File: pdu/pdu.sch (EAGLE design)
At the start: 54 parts, among them IC1 FDN359BN, IC2 FDN359BN, IC3 FDN359BN, J1 S2B-PH-K-S(LF)(SN), J10 S2B-PH-K-S(LF)(SN), J2 S2B-PH-K-S(LF)(SN), J3 S2B-PH-K-S(LF)(SN), J4 S2B-PH-K-S(LF)(SN), J5 S2B-PH-K-S(LF)(SN), J6 S2B-PH-K-S(LF)(SN), J7 S2B-PH-K-S(LF)(SN), J8 S2B-PH-K-S(LF)(SN), J9 S2B-PH-K-S(LF)(SN)

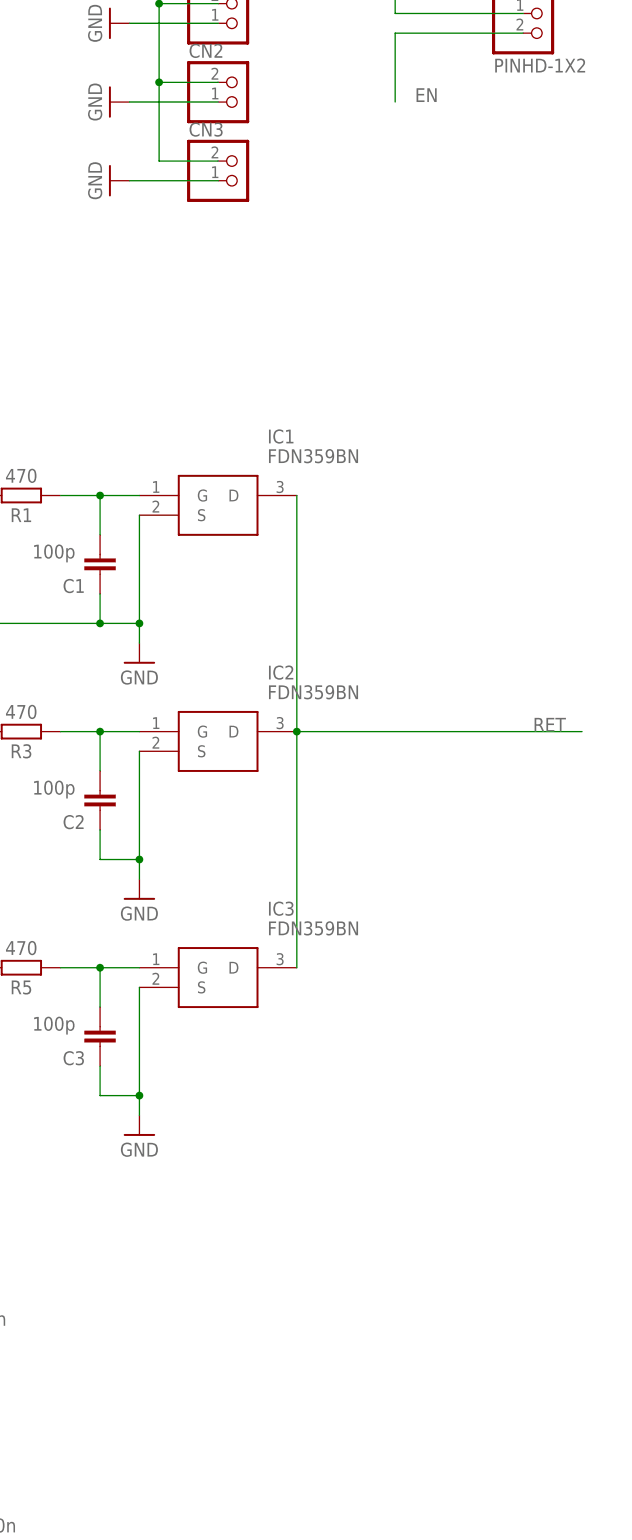
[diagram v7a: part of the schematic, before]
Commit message: add status leds
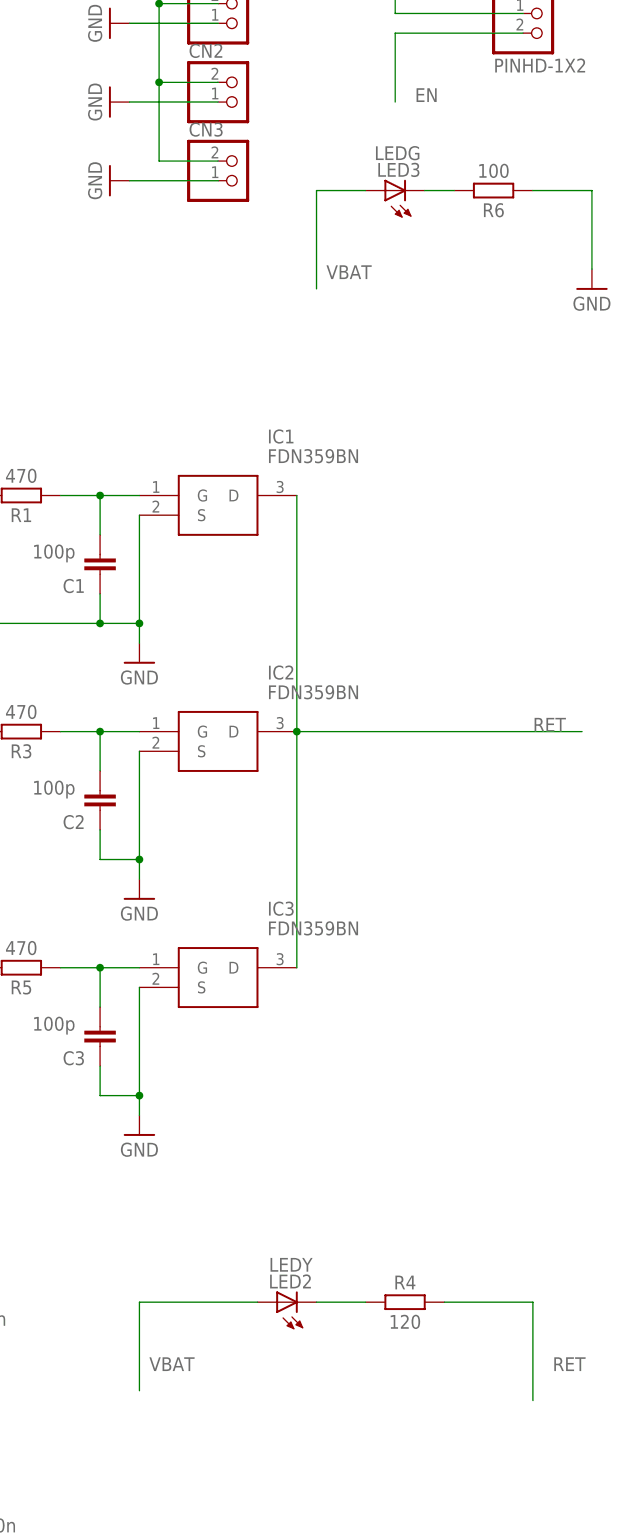
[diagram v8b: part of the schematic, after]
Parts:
- added LED2: LEDY, adafruit:LEDCHIPLED_0805
- added LED3: LEDG, adafruit:LEDCHIPLED_0805
- added R4: 120, Resistor:R_CHIP-0603(1608-METRIC)
- added R6: 100, Resistor:R_CHIP-0603(1608-METRIC)
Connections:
- new net N$4: LED3.C, R6.2
- new net N$5: LED2.C, R4.1
- net GND: now also R6.1
- net RET: now also R4.2
- net VBAT: now also LED2.A, LED3.A
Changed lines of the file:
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@@
 <part name="J9" library="Connectors" library_urn="urn:adsk.eagle:library:28493002" deviceset="S2B-PH-K-S(LF)(SN)" device="" package3d_urn="urn:adsk.eagle:package:10989924/2"/>
 <part name="J10" library="Connectors" library_urn="urn:adsk.eagle:library:28493002" deviceset="S2B-PH-K-S(LF)(SN)" device="" package3d_urn="urn:adsk.eagle:package:10989924/2"/>
+<part name="LED2" library="adafruit" library_urn="urn:adsk.eagle:library:420" deviceset="LED" device="CHIPLED_0805" package3d_urn="urn:adsk.eagle:package:6240559/1" value="LEDY"/>
+<part name="R4" library="Resistor" library_urn="urn:adsk.eagle:library:16378527" deviceset="R" device="CHIP-0603(1608-METRIC)" package3d_urn="urn:adsk.eagle:package:16378565/5" technology="_" value="120"/>
+<part name="R6" library="Resistor" library_urn="urn:adsk.eagle:library:16378527" deviceset="R" device="CHIP-0603(1608-METRIC)" package3d_urn="urn:adsk.eagle:package:16378565/5" technology="_" value="100"/>
+<part name="LED3" library="adafruit" library_urn="urn:adsk.eagle:library:420" deviceset="LED" device="CHIPLED_0805" package3d_urn="urn:adsk.eagle:package:6240559/1" value="LEDG"/>
+<part name="SUPPLY7" library="Power_Symbols" library_urn="urn:adsk.eagle:library:16502351" deviceset="GND-BAR" device="" value="GND"/>
 </parts>
 <sheets>
@@
 <attribute name="NAME" x="2.54" y="-235.712" size="1.778" layer="95" rot="R180"/>
 <attribute name="VALUE" x="2.54" y="-224.79" size="1.778" layer="96" rot="R180"/>
+</instance>
+<instance part="LED2" gate="G$1" x="17.78" y="-104.14" smashed="yes" rot="R90">
+<attribute name="NAME" x="22.352" y="-100.584" size="1.778" layer="95" rot="R180"/>
+<attribute name="VALUE" x="22.352" y="-98.425" size="1.778" layer="96" rot="R180"/>
+</instance>
+<instance part="R4" gate="G$1" x="34.29" y="-104.14" smashed="yes">
+<attribute name="NAME" x="34.29" y="-101.6" size="1.778" layer="95" align="center"/>
+<attribute name="VALUE" x="34.29" y="-106.68" size="1.778" layer="96" align="center"/>
+</instance>
+<instance part="R6" gate="G$1" x="45.72" y="39.37" smashed="yes" rot="R180">
+<attribute name="NAME" x="45.72" y="36.83" size="1.778" layer="95" rot="R180" align="center"/>
+<attribute name="VALUE" x="45.72" y="41.91" size="1.778" layer="96" rot="R180" align="center"/>
+</instance>
+<instance part="LED3" gate="G$1" x="31.75" y="39.37" smashed="yes" rot="R90">
+<attribute name="NAME" x="36.322" y="42.926" size="1.778" layer="95" rot="R180"/>
+<attribute name="VALUE" x="36.322" y="45.085" size="1.778" layer="96" rot="R180"/>
+</instance>
+<instance part="SUPPLY7" gate="G$1" x="58.42" y="26.67" smashed="yes">
+<attribute name="VALUE" x="58.42" y="24.765" size="1.778" layer="96" align="center"/>
 </instance>
 </instances>
@@
 <wire x1="-5.08" y1="-77.47" x2="0" y2="-77.47" width="0.1524" layer="91"/>
 <junction x="0" y="-77.47"/>
+</segment>
+<segment>
+<pinref part="R6" gate="G$1" pin="1"/>
+<wire x1="50.8" y1="39.37" x2="58.42" y2="39.37" width="0.1524" layer="91"/>
+<pinref part="SUPPLY7" gate="G$1" pin="GND"/>
+<wire x1="58.42" y1="39.37" x2="58.42" y2="29.21" width="0.1524" layer="91"/>
 </segment>
 </net>
@@
 <junction x="35.56" y="-203.2"/>
 <pinref part="J9" gate="G$1" pin="2"/>
+</segment>
+<segment>
+<pinref part="LED3" gate="G$1" pin="A"/>
+<wire x1="29.21" y1="39.37" x2="22.86" y2="39.37" width="0.1524" layer="91"/>
+<wire x1="22.86" y1="39.37" x2="22.86" y2="26.67" width="0.1524" layer="91"/>
+<label x="24.13" y="27.94" size="1.778" layer="95"/>
+</segment>
+<segment>
+<pinref part="LED2" gate="G$1" pin="A"/>
+<wire x1="15.24" y1="-104.14" x2="0" y2="-104.14" width="0.1524" layer="91"/>
+<wire x1="0" y1="-104.14" x2="0" y2="-115.57" width="0.1524" layer="91"/>
+<label x="1.27" y="-113.03" size="1.778" layer="95"/>
 </segment>
 </net>
@@
 <wire x1="13.97" y1="-205.74" x2="13.97" y2="-220.98" width="0.1524" layer="91"/>
 </segment>
-</net>
+<segment>
+<pinref part="R4" gate="G$1" pin="2"/>
+<wire x1="39.37" y1="-104.14" x2="50.8" y2="-104.14" width="0.1524" layer="91"/>
+<wire x1="50.8" y1="-104.14" x2="50.8" y2="-116.84" width="0.1524" layer="91"/>
+<label x="53.34" y="-113.03" size="1.778" layer="95"/>
+</segment>
+</net>
+<net name="N$4" class="0">
+<segment>
+<pinref part="LED3" gate="G$1" pin="C"/>
+<pinref part="R6" gate="G$1" pin="2"/>
+<wire x1="36.83" y1="39.37" x2="40.64" y2="39.37" width="0.1524" layer="91"/>
+</segment>
+</net>
+<net name="N$5" class="0">
+<segment>
+<pinref part="LED2" gate="G$1" pin="C"/>
+<pinref part="R4" gate="G$1" pin="1"/>
+<wire x1="22.86" y1="-104.14" x2="29.21" y2="-104.14" width="0.1524" layer="91"/>
+</segment>
+</net>
